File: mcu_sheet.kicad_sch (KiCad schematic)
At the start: 22 parts, among them IC1 STM32H523CET6, J1 Conn_01x05, J3 Conn_01x04, SW1 SW_SPDT, SW2 SW_Push, Y1 Crystal

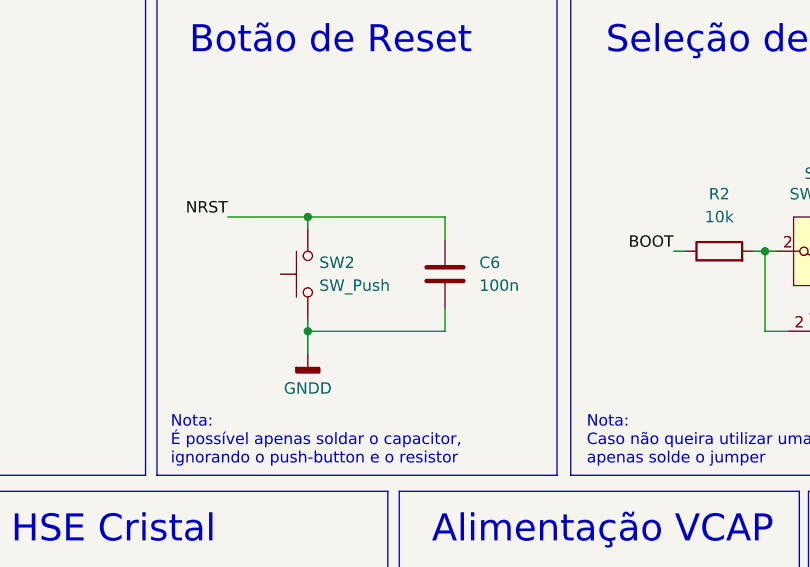
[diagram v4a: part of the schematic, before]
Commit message: Removi o botao de reset do design
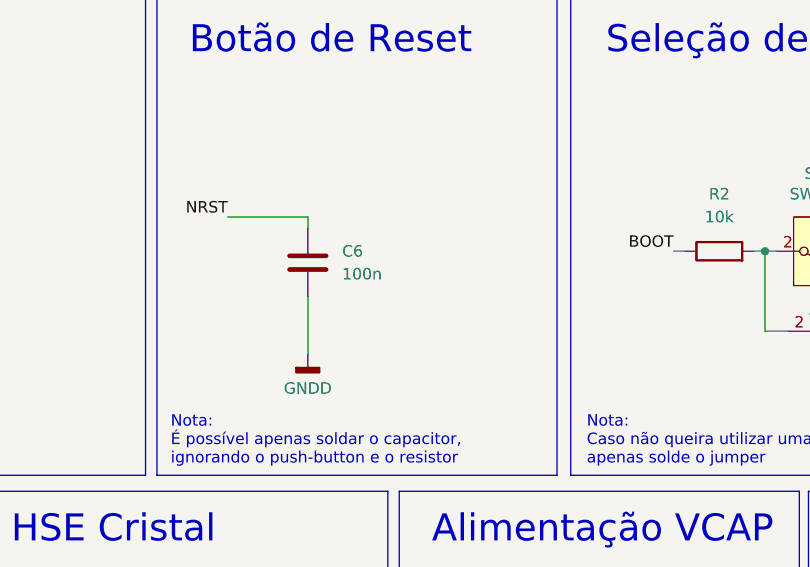
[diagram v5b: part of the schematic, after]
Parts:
- removed SW2: SW_Push, Button_Switch_SMD:SW_SPST_CK_RS282G05A3, symbol Switch:SW_Push
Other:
- moved on the sheet: C6
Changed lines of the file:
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@@
 	)
 	(junction
-		(at 176.53 53.34)
-		(diameter 0)
-		(color 0 0 0 0)
-	)
-	(junction
 		(at 227.33 44.45)
 		(diameter 0)
@@
 	)
 	(junction
-		(at 176.53 40.64)
-		(diameter 0)
-		(color 0 0 0 0)
-	)
-	(junction
 		(at 52.07 158.75)
 		(diameter 0)
@@
 	(wire
 		(pts
-			(xy 176.53 53.34) (xy 176.53 52.07)
+			(xy 176.53 49.53) (xy 176.53 55.88)
 		)
 		(stroke
@@
 	(wire
 		(pts
-			(xy 176.53 40.64) (xy 191.77 40.64)
-		)
-		(stroke
-			(width 0)
-			(type default)
-		)
-	)
-	(wire
-		(pts
 			(xy 41.91 50.8) (xy 53.34 50.8)
 		)
@@
 	(wire
 		(pts
-			(xy 176.53 53.34) (xy 191.77 53.34)
-		)
-		(stroke
-			(width 0)
-			(type default)
-		)
-	)
-	(wire
-		(pts
 			(xy 251.46 95.25) (xy 255.27 95.25)
 		)
@@
 	(wire
 		(pts
-			(xy 176.53 53.34) (xy 176.53 55.88)
-		)
-		(stroke
-			(width 0)
-			(type default)
-		)
-	)
-	(wire
-		(pts
 			(xy 199.39 96.52) (xy 199.39 92.71)
 		)
@@
 	(wire
 		(pts
-			(xy 191.77 43.18) (xy 191.77 40.64)
+			(xy 176.53 41.91) (xy 176.53 40.64)
 		)
 		(stroke
@@
 	(wire
 		(pts
-			(xy 191.77 53.34) (xy 191.77 50.8)
-		)
-		(stroke
-			(width 0)
-			(type default)
-		)
-	)
-	(wire
-		(pts
 			(xy 251.46 100.33) (xy 255.27 100.33)
 		)
@@
 	(wire
 		(pts
-			(xy 176.53 40.64) (xy 176.53 41.91)
-		)
-		(stroke
-			(width 0)
-			(type default)
-		)
-	)
-	(wire
-		(pts
 			(xy 52.07 83.82) (xy 52.07 85.09)
 		)
@@
 	)
 	(symbol
-		(lib_id "Switch:SW_Push")
-		(at 176.53 46.99 90)
-		(unit 1)
-		(exclude_from_sim no)
-		(in_bom yes)
-		(on_board yes)
-		(dnp no)
-		(fields_autoplaced yes)
-		(property "Reference" "SW2"
-			(at 177.8 45.7199 90)
-			(effects
-				(font
-					(size 1.27 1.27)
-				)
-				(justify right)
-			)
-		)
-		(property "Value" "SW_Push"
-			(at 177.8 48.2599 90)
-			(effects
-				(font
-					(size 1.27 1.27)
-				)
-				(justify right)
-			)
-		)
-		(property "Footprint" "Button_Switch_SMD:SW_SPST_CK_RS282G05A3"
-			(at 171.45 46.99 0)
-			(effects
-				(font
-					(size 1.27 1.27)
-				)
-				(hide yes)
-			)
-		)
-		(property "Datasheet" "~"
-			(at 171.45 46.99 0)
-			(effects
-				(font
-					(size 1.27 1.27)
-				)
-				(hide yes)
-			)
-		)
-		(property "Description" "Push button switch, generic, two pins"
-			(at 176.53 46.99 0)
-			(effects
-				(font
-					(size 1.27 1.27)
-				)
-				(hide yes)
-			)
-		)
-		(pin "1"
-		)
-		(pin "2"
-		)
-		(instances
-			(project ""
-				(path "/089184b8-f600-4584-b3f1-b59eb16eefc1/6eb5fc8d-8b20-48b4-b65b-6d065ff48b2f"
-					(reference "SW2")
-					(unit 1)
-				)
-			)
-		)
-	)
-	(symbol
 		(lib_id "Device:C")
 		(at 170.18 96.52 0)
@@
 	(symbol
 		(lib_id "Device:C")
-		(at 191.77 46.99 0)
+		(at 176.53 45.72 0)
 		(unit 1)
 		(exclude_from_sim no)
@@
 		(fields_autoplaced yes)
 		(property "Reference" "C6"
-			(at 195.58 45.7199 0)
+			(at 180.34 44.4499 0)
 			(effects
 				(font
@@
 		)
 		(property "Value" "100n"
-			(at 195.58 48.2599 0)
+			(at 180.34 46.9899 0)
 			(effects
 				(font
@@
 		)
 		(property "Footprint" "Capacitor_SMD:C_0603_1608Metric_Pad1.08x0.95mm_HandSolder"
-			(at 192.7352 50.8 0)
+			(at 177.4952 49.53 0)
 			(effects
 				(font
@@
 		)
 		(property "Datasheet" "~"
-			(at 191.77 46.99 0)
+			(at 176.53 45.72 0)
 			(effects
 				(font
@@
 		)
 		(property "Description" "Unpolarized capacitor"
-			(at 191.77 46.99 0)
+			(at 176.53 45.72 0)
 			(effects
 				(font

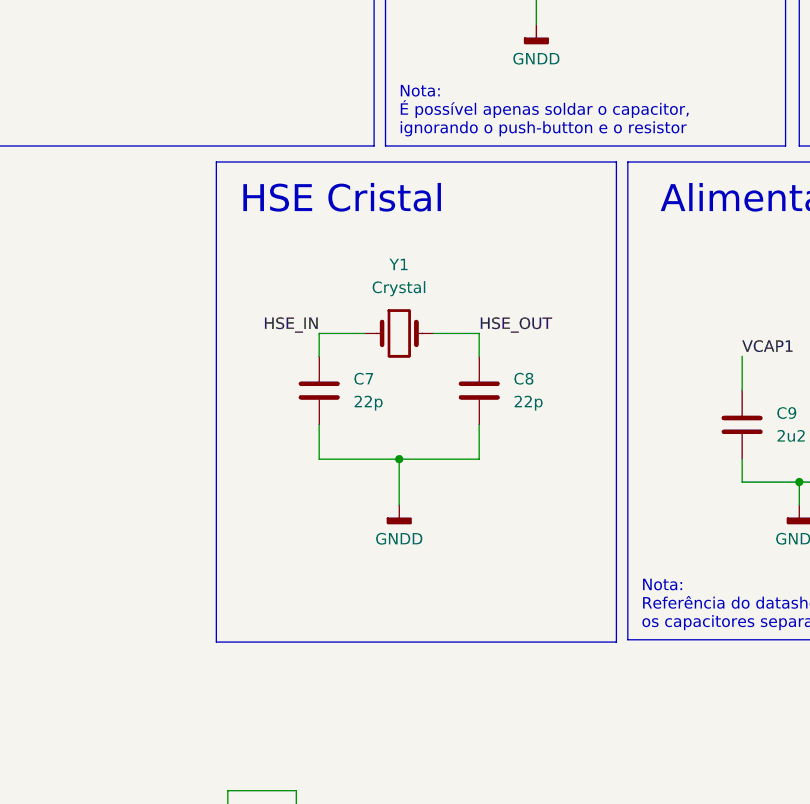
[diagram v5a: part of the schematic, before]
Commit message: Troquei o conector para o conector DEUTSCH
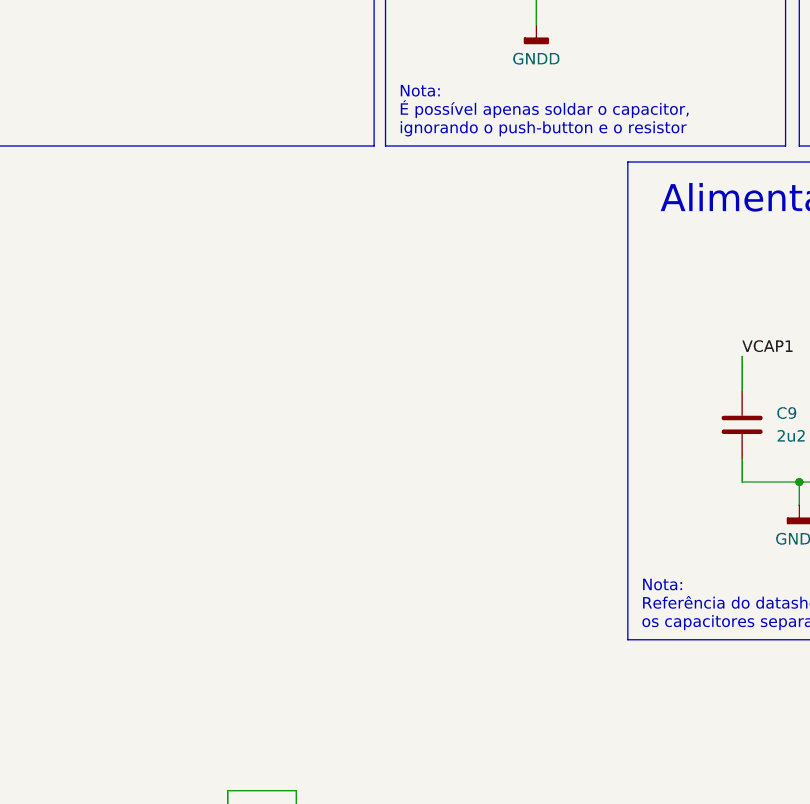
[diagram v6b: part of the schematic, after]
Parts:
- removed C7, C8: 22p, Capacitor_SMD:C_0603_1608Metric_Pad1.08x0.95mm_HandSolder, symbol Device:C
- removed Y1: Crystal, Crystal:Crystal_SMD_HC49-SD_HandSoldering, symbol Device:Crystal
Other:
- note removed: "HSE Cristal"
